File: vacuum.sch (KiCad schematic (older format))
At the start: 69 parts, among them J1 к БП, J10 геркон шибера 1, J11 запасной, J12 запасной, J13 к БП, J2 нагрузка, J3 нагрузка, J4 геркон клапана 0, J5 нагрузка, J6 нагрузка, J7 к БП, J8 геркон клапана 1, J9 геркон шибера 0, Q1 IRF740, Q2 IRF740, Q3 IRF740, Q4 IRF740, SW1 Кнопка, SW2 Кнопка, SW3 Кнопка, SW4 Выключить автоматику, SW5 Кнопка, U1 PC817, U10 PC817, U2 PC817, U3 PC817, U4 PC817, U5 PC817, U6 PC817, U7 PC817, U8 PC817, U9 PC817

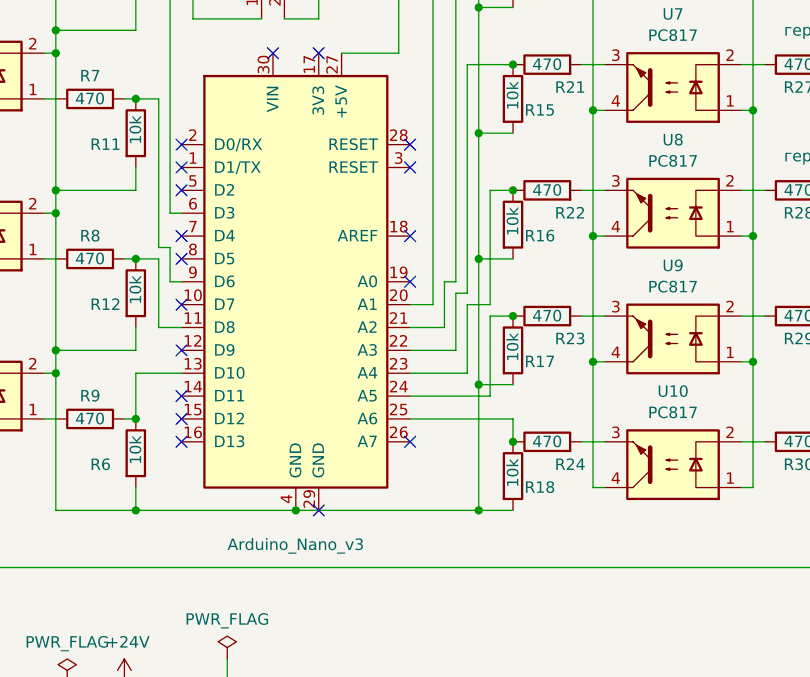
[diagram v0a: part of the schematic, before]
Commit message: capasitor added to reset pin of Arduino dor DTR disabling
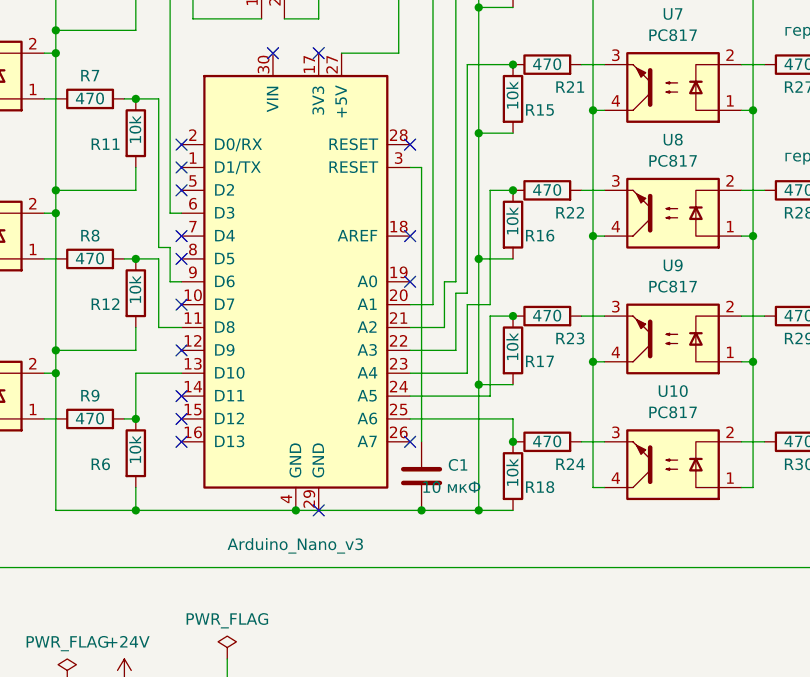
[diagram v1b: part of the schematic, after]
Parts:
- added C1: 10 мкФ, Capacitor_THT:C_Disc_D6.0mm_W2.5mm_P5.00mm, symbol Device:C
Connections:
- net at A1.3 (RESET): now also C1.1
- net at A1.4 (GND), J13.1 (Pin_1), R10.2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: now also C1.2
- no-connect marks 18 -> 17
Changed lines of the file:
@@
 $EndComp
 NoConn ~ 5450 4500
-NoConn ~ 5450 4600
 NoConn ~ 5450 4900
 NoConn ~ 5450 5800
@@
 Connection ~ 4950 6100
 Wire Wire Line
-	4950 6100 5750 6100
+	4950 6100 5500 6100
 Wire Wire Line
 	5450 5600 5800 5600
@@
 Wire Wire Line
 	2500 6200 2400 6200
+$Comp
+L Device:C C1
+U 1 1 5D37D26C
+P 5500 5950
+F 0 "C1" H 5615 5997 50  0000 L CNN
+F 1 "10 мкФ" H 5500 5900 50  0000 L CNN
+F 2 "Capacitor_THT:C_Disc_D6.0mm_W2.5mm_P5.00mm" H 5538 5800 50  0001 C CNN
+F 3 "~" H 5500 5950 50  0001 C CNN
+	1    5500 5950
+	1    0    0    -1
+$EndComp
+Connection ~ 5500 6100
+Wire Wire Line
+	5500 6100 5750 6100
+Wire Wire Line
+	5450 4600 5500 4600
+Wire Wire Line
+	5500 4600 5500 5800
 $EndSCHEMATC

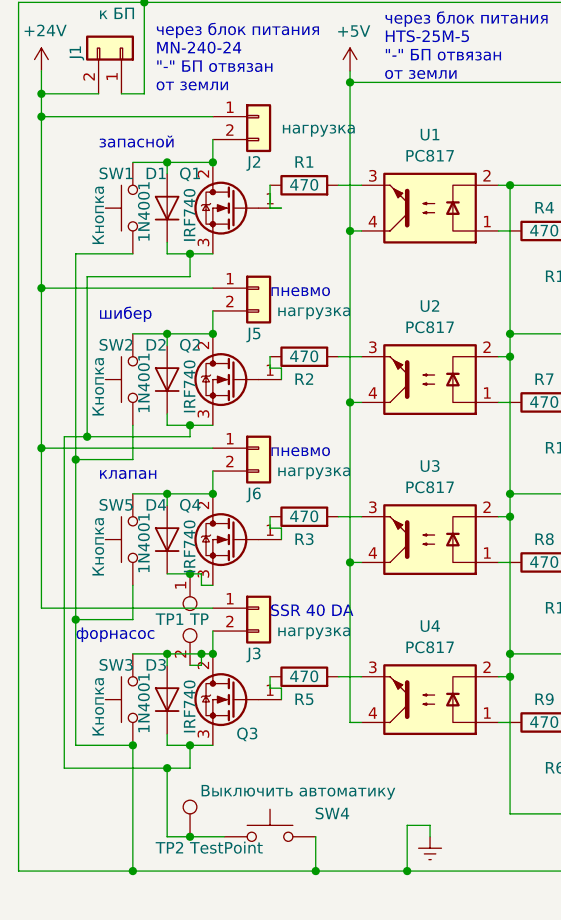
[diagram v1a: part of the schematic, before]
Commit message: diods direction changed to correct
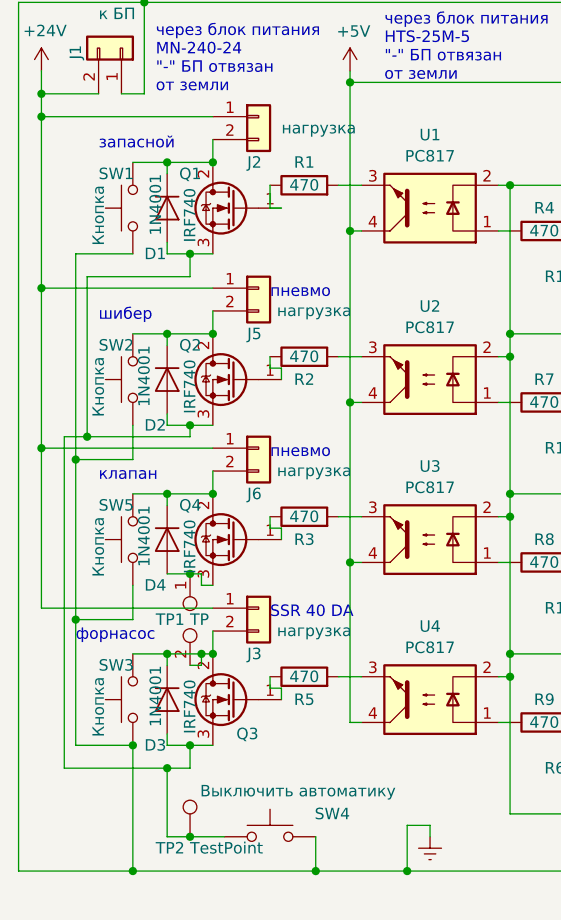
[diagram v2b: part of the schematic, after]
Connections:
- net at J3.2 (Pin_2), Q3.2 (D), SW3.2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: now also D3.1 (K); no longer D3.2 (A)
- net at Q1.3 (S), Q2.3 (S), Q3.3 (S)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: now also D1.2 (A), D2.2 (A), D3.2 (A); no longer D1.1 (K), D2.1 (K), D3.1 (K)
- net at Q4.3 (S), TP1.1: now also D4.2 (A); no longer D4.1 (K)
- net at J6.2 (Pin_2), Q4.2 (D), SW5.2: now also D4.1 (K); no longer D4.2 (A)
- net at J5.2 (Pin_2), Q2.2 (D), SW2.2: now also D2.1 (K); no longer D2.2 (A)
- net at J2.2 (Pin_2), Q1.2 (D), SW1.2: now also D1.1 (K); no longer D1.2 (A)
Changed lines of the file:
@@
 U 1 1 5D2916F9
 P 2400 5600
-F 0 "D3" V 2550 5600 50  0000 L CNN
-F 1 "1N4001" H 2250 5700 50  0000 L CNN
+F 0 "D3" V 2600 5500 50  0000 L CNN
+F 1 "1N4001" H 2250 5550 50  0000 L CNN
 F 2 "Diode_THT:D_DO-41_SOD81_P10.16mm_Horizontal" H 2400 5425 50  0001 C CNN
 F 3 "http://www.vishay.com/docs/88503/1n4001.pdf" H 2400 5600 50  0001 C CNN
 	1    2400 5600
-	0    -1   -1   0
+	0    1    1    0
 $EndComp
 Wire Wire Line
@@
 U 1 1 5D3A8EDB
 P 2400 3450
-F 0 "D1" V 2550 3450 50  0000 L CNN
-F 1 "1N4001" H 2250 3550 50  0000 L CNN
+F 0 "D1" V 2600 3350 50  0000 L CNN
+F 1 "1N4001" H 2250 3400 50  0000 L CNN
 F 2 "Diode_THT:D_DO-41_SOD81_P10.16mm_Horizontal" H 2400 3275 50  0001 C CNN
 F 3 "http://www.vishay.com/docs/88503/1n4001.pdf" H 2400 3450 50  0001 C CNN
 	1    2400 3450
-	0    -1   -1   0
+	0    1    1    0
 $EndComp
 Wire Wire Line
@@
 U 1 1 5D2F61BD
 P 2400 4900
-F 0 "D4" V 2550 4900 50  0000 L CNN
-F 1 "1N4001" H 2250 5000 50  0000 L CNN
+F 0 "D4" V 2600 4800 50  0000 L CNN
+F 1 "1N4001" H 2250 4800 50  0000 L CNN
 F 2 "Diode_THT:D_DO-41_SOD81_P10.16mm_Horizontal" H 2400 4725 50  0001 C CNN
 F 3 "http://www.vishay.com/docs/88503/1n4001.pdf" H 2400 4900 50  0001 C CNN
 	1    2400 4900
-	0    -1   -1   0
+	0    1    1    0
 $EndComp
 Connection ~ 2600 4000
@@
 U 1 1 5D316E84
 P 2400 4200
-F 0 "D2" V 2550 4200 50  0000 L CNN
-F 1 "1N4001" H 2250 4300 50  0000 L CNN
+F 0 "D2" V 2600 4100 50  0000 L CNN
+F 1 "1N4001" H 2250 4100 50  0000 L CNN
 F 2 "Diode_THT:D_DO-41_SOD81_P10.16mm_Horizontal" H 2400 4025 50  0001 C CNN
 F 3 "http://www.vishay.com/docs/88503/1n4001.pdf" H 2400 4200 50  0001 C CNN
 	1    2400 4200
-	0    -1   -1   0
-$EndComp
-Wire Wire Line
+	0    1    1    0
+$EndComp
+Wire Wire Line
